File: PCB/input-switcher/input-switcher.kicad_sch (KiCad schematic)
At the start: 3 parts, among them U1 CD4052B

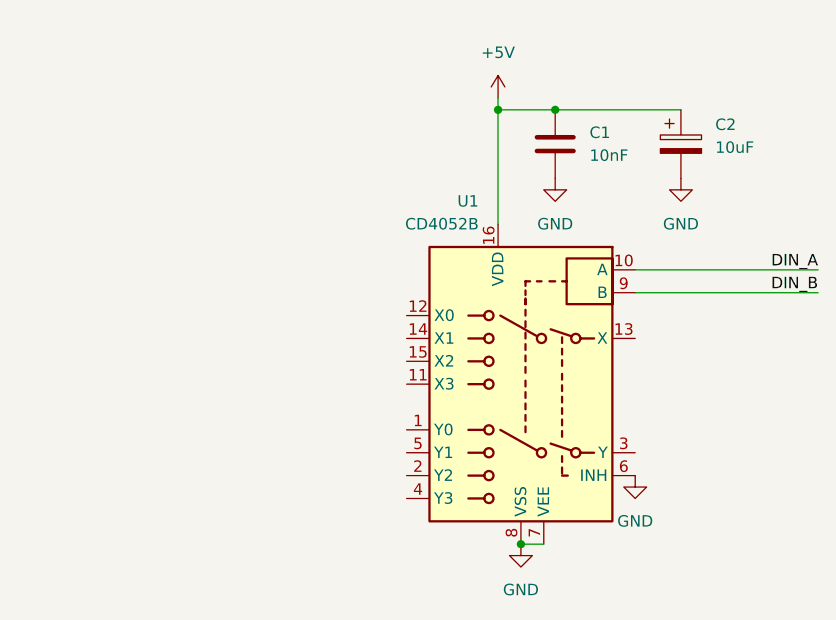
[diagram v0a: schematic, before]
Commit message: add schematic for input switcher
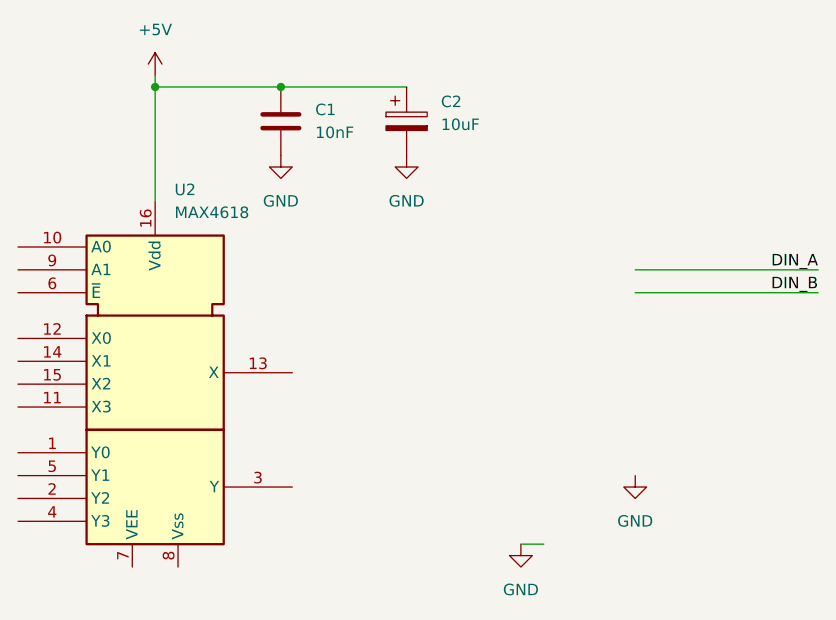
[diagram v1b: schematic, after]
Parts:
- removed U1: CD4052B, symbol Analog_Switch:CD4052B
- added U2: MAX4618, symbol 4xxx_IEEE:4052
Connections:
- net +5V: now also U2.16 (Vdd)
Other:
- moved on the sheet: C1, C2

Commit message: input board schematic update
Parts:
- removed U2: MAX4618, symbol 4xxx_IEEE:4052
- added C3: 10nF, Capacitor_THT:C_Disc_D6.0mm_W2.5mm_P5.00mm, symbol Device:C
- added C4: 10uF, Capacitor_THT:C_Rect_L7.0mm_W2.5mm_P5.00mm, symbol Device:C_Polarized
- added J1, J2, J3, J4: Conn_Coaxial_x2, symbol Connector:Conn_Coaxial_x2
- added J5: Screw_Terminal_01x04, symbol Connector:Screw_Terminal_01x04
- added J6, J7: Screw_Terminal_01x03, symbol Connector:Screw_Terminal_01x03
- added U1: CD4052B, symbol Analog_Switch:CD4052B
- C1: footprint (none) -> Capacitor_THT:C_Disc_D6.0mm_W2.5mm_P5.00mm; Mouser PN (none) -> 791-YV101103Z60HAND5
- C2: footprint (none) -> Capacitor_THT:C_Rect_L7.0mm_W2.5mm_P5.00mm; Mouser PN (none) -> 810-FG28X5R1E106MR06
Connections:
- net +5V: now also J7.1 (Pin_1), U1.16 (VDD)
- net GND: now also C3.1, C4.1, J1.3 (EXT), J2.3 (EXT), J3.3 (EXT), J4.3 (EXT), J5.4 (Pin_4), J6.3 (Pin_3), J7.2 (Pin_2), U1.8 (VSS)
- new net -5V: C3.2, C4.2, J7.3 (Pin_3), U1.7 (VEE)
- new net CH1L: J1.1 (IN1), U1.12 (X0)
- new net CH1R: J1.2 (IN2), U1.1 (Y0)
- new net CH2L: J2.1 (IN1), U1.14 (X1)
- new net CH2R: J2.2 (IN2), U1.5 (Y1)
- new net CH3L: J3.1 (IN1), U1.15 (X2)
- new net CH3R: J3.2 (IN2), U1.2 (Y2)
- new net CH4L: J4.1 (IN1), U1.11 (X3)
- new net CH4R: J4.2 (IN2), U1.4 (Y3)
- new net CTRL_A: J5.1 (Pin_1), U1.10 (A)
- new net CTRL_B: J5.2 (Pin_2), U1.9 (B)
- new net MUTE: J5.3 (Pin_3), U1.6 (INH)
- new net OUT_L: J6.1 (Pin_1), U1.13 (X)
- new net OUT_R: J6.2 (Pin_2), U1.3 (Y)
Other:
- moved on the sheet: C1, C2

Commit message: lots of schematic + pcb updates
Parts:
- removed J1, J2, J3, J4: Conn_Coaxial_x2, symbol Connector:Conn_Coaxial_x2
- added J1: PJRAS4X2U01AUX, PJRAS4X2U01AUX, symbol PJRAS4X2U01AUX:PJRAS4X2U01AUX
- C1, C3: value 10nF -> 100nF; Mouser PN 791-YV101103Z60HAND5 -> 791-RD21B104K500A5HA
- J2: renamed from J5; footprint (none) -> Connector_Phoenix_MSTB:PhoenixContact_MSTBA_2,5_4-G-5,08_1x04_P5.08mm_Horizontal; Mouser PN (none) -> 651-1757268
- J3: renamed from J6; footprint (none) -> Connector_Phoenix_MSTB:PhoenixContact_MSTBA_2,5_3-G-5,08_1x03_P5.08mm_Horizontal; Mouser PN (none) -> 651-1757255
- J4: renamed from J7; footprint (none) -> TerminalBlock_CUI:TerminalBlock_CUI_TB007-508-03_1x03_P5.08mm_Horizontal; Mouser PN (none) -> 490-TB007-508-03BE
- U1: footprint (none) -> Package_DIP:DIP-16_W7.62mm_Socket; Mouser PN (none) -> 595-CD4052BE
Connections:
- net CH1L: now also J1.T12 (IN2)
- net CH1R: now also J1.T11 (IN1)
- net CH2L: now also J1.T22 (IN2)
- net CH2R: now also J1.T21 (IN1)
- net CH3L: now also J1.T32 (IN2)
- net CH3R: now also J1.T31 (IN1)
- net CH4L: now also J1.T42 (IN2)
- net CH4R: now also J1.T41 (IN1)
- net GND: now also J1.S1 (EXT), J1.S2 (EXT), J1.S3 (EXT), J1.S4 (EXT)
